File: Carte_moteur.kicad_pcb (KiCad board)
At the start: 2 copper layers, 111 parts, among them J101 Conn_01x02_Socket, J102 Conn_01x02, J103 Conn_01x02, J104 Conn_01x07, J105 Conn_01x02_Socket, J106 Conn_01x07, J201 Conn_01x05_Pin, J202 Conn_01x04_Pin, J301 Conn_01x05_Pin, J302 Conn_01x04_Pin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

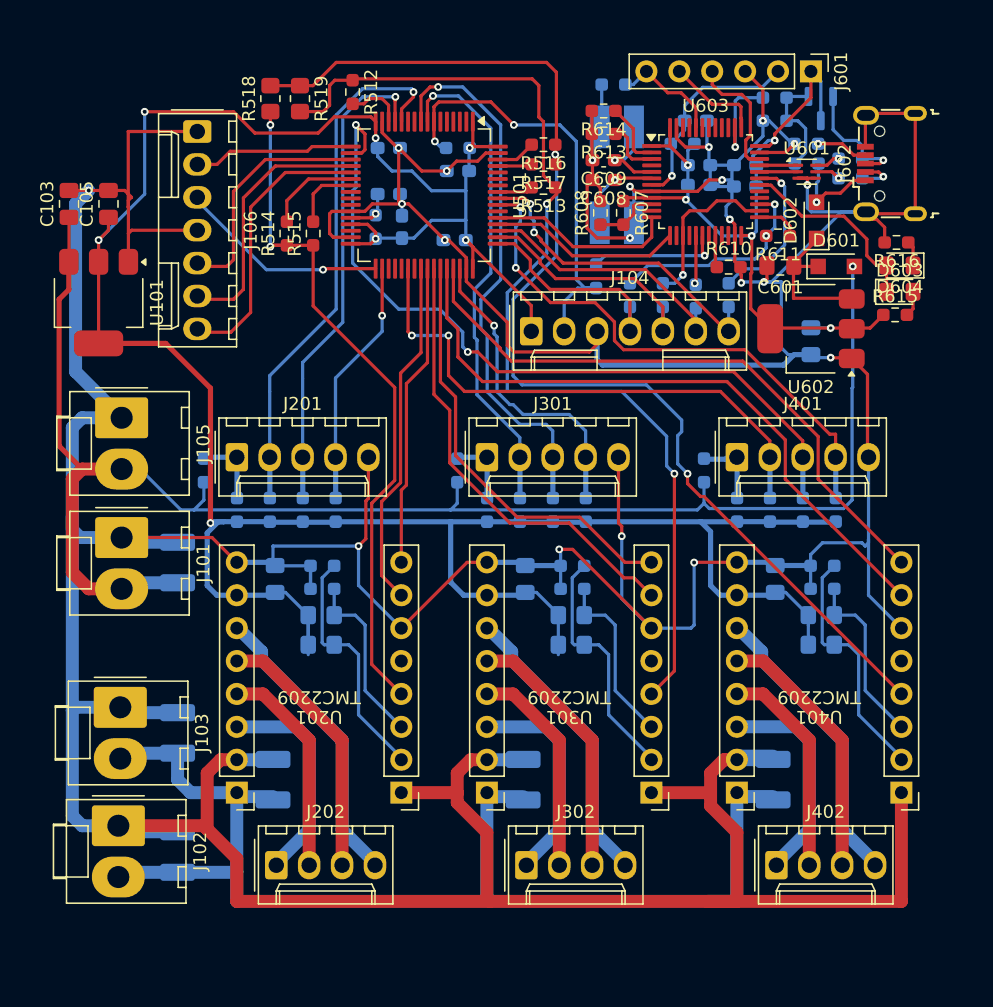
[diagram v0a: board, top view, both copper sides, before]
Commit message: silk and holes ok
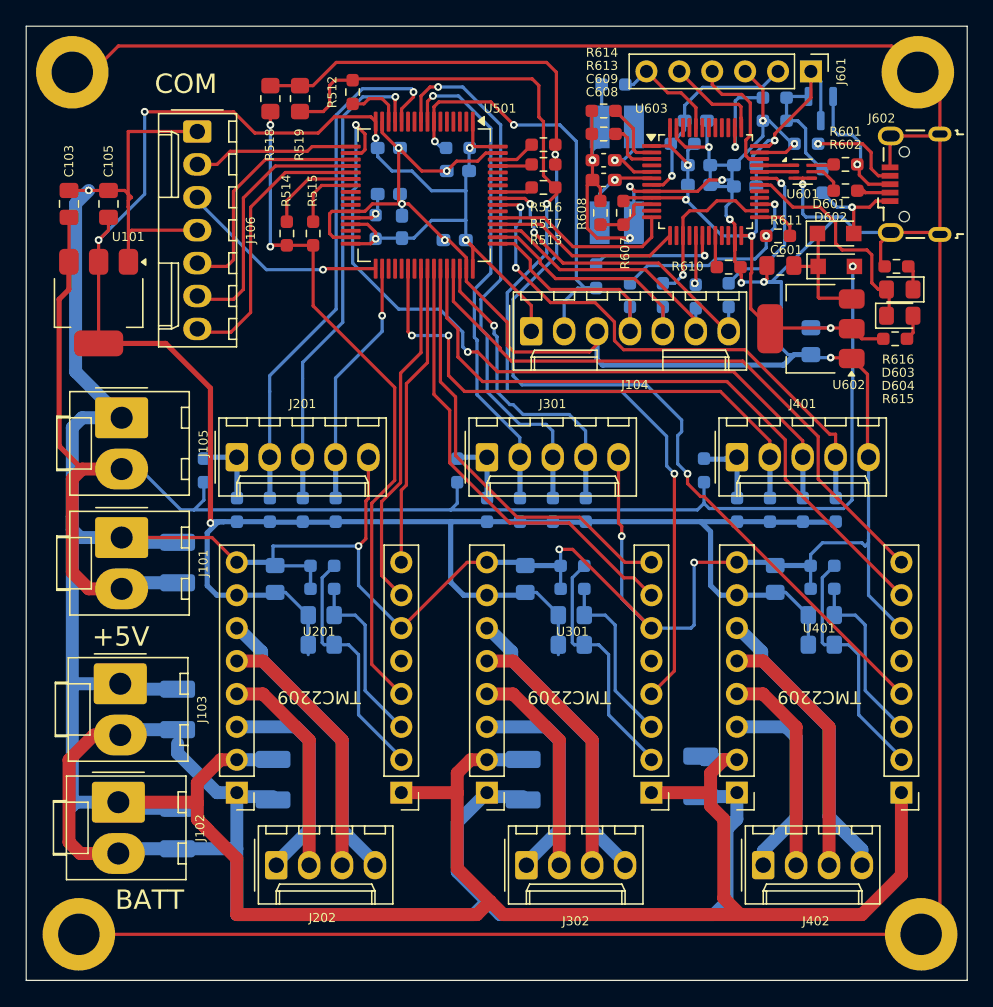
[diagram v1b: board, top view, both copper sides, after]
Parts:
- added H101: MountingHole_Pad, MountingHole:MountingHole_3.2mm_M3_DIN965_Pad, F.Cu at (79.5, 97.0)
- added H102: MountingHole_Pad, MountingHole:MountingHole_3.2mm_M3_DIN965_Pad, F.Cu at (144.8, 97.0)
- added H103: MountingHole_Pad, MountingHole:MountingHole_3.2mm_M3_DIN965_Pad, F.Cu at (80.0, 163.6)
- added H104: MountingHole_Pad, MountingHole:MountingHole_3.2mm_M3_DIN965_Pad, F.Cu at (145.0, 163.6)
- R601, R602: moved to F.Cu
- moved C401 5.59 mm to (128.0, 151.4)
- moved J602 2.48 mm to (144.5, 105.7)
- moved D603 1.85 mm to (143.4, 115.8)
- moved D604 1.85 mm to (143.4, 113.8)
- moved R615 1.85 mm to (143.0, 117.6)
- moved R616 1.85 mm to (143.1, 112.0)
- moved J103 1.82 mm to (83.2, 144.2)
- moved C102 1.82 mm to (87.6, 146.2)
- moved C104 1.82 mm to (87.6, 155.4)
- moved J102 1.82 mm to (83.1, 153.4)
- moved R604 1.81 mm to (137.4, 105.4), turned to 90 degrees
- moved D602 1.79 mm to (138.4, 109.5), turned to 0 degrees
- moved R602 1.03 mm to (139.2, 106.2)
- moved J402 1.02 mm to (132.8, 158.2)
- moved R601 0.59 mm to (139.2, 104.1)
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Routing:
- net GND: track 561.1 -> 743.8 mm
- net +BATT: track 91.1 -> 110.2 mm
- net Net-(J602-ID): track 4.01 -> 7.31 mm
- net Net-(D601-K): track 11.7 -> 8.97 mm
- net /stlink/LED: track 15.1 -> 17.1 mm
- net Net-(J602-D+): track 10.1 -> 10.8 mm
- net /tmc_motor2/A02: track 16.4 -> 15.7 mm
- net Net-(U601-D+_out): track 1.99 -> 1.33 mm, vias 1 -> 0
- net Net-(Q601-B): track 8.14 -> 8.74 mm
- net Net-(U601-D-_out): track 1.99 -> 2.39 mm, vias 1 -> 0
- net Net-(J602-D-): track 3.21 -> 2.95 mm, vias 1 -> 0
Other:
- board outline added: 72.6 x 73.7 mm
- board text added: "+5V"
- board text added: "BATT"
- board text added: "COM"

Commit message: ready for manufacturing
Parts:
- moved R518 1.65 mm to (94.8, 97.4)
- moved R519 1.65 mm to (97.1, 97.4)
- moved R512 0.51 mm to (101.1, 98.0)
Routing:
- net GND: track 743.8 -> 1265.2 mm, vias 21 -> 67
- net /micro/TMC1: track 53.9 -> 61.2 mm
- net /micro/TMC2: track 80.7 -> 78.3 mm
- net /micro/TMC3: track 91.8 -> 89.5 mm
- net /micro/TIM3_CH1: track 42.3 -> 44.5 mm
- net /micro/HRTIM_CHA1: track 35.3 -> 37.1 mm
- net /micro/TIM3_CH2: track 59.7 -> 61.3 mm
- net /micro/HRTIM_CHA2: track 33.4 -> 34.8 mm
- net /micro/T_SWDIO: track 17.5 -> 16.2 mm
- net /micro/TIM1_ETR: track 24.0 -> 22.8 mm
- net /micro/TIM5_CH1: track 41.3 -> 42.4 mm
- net /micro/T_SWCLK: track 19.7 -> 18.7 mm
- net /micro/SPI1_SCK: track 18.1 -> 19.0 mm
- net /micro/HRTIM_CHB1: track 50.8 -> 51.6 mm
- net /micro/TIM1_CH2: track 42.7 -> 42.1 mm
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- added copper zone on B.Cu, net GND
- added copper zone on F.Cu, net GND

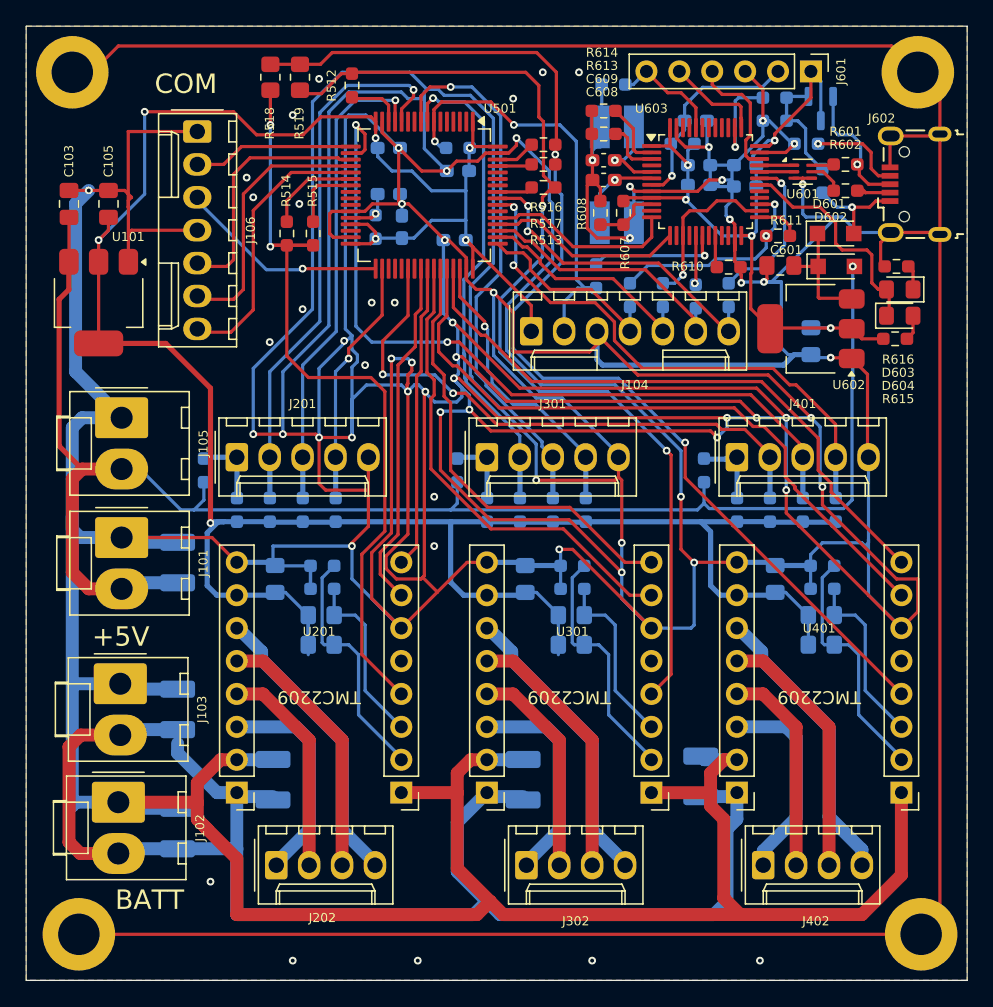
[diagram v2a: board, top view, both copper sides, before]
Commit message: remove wierd angles
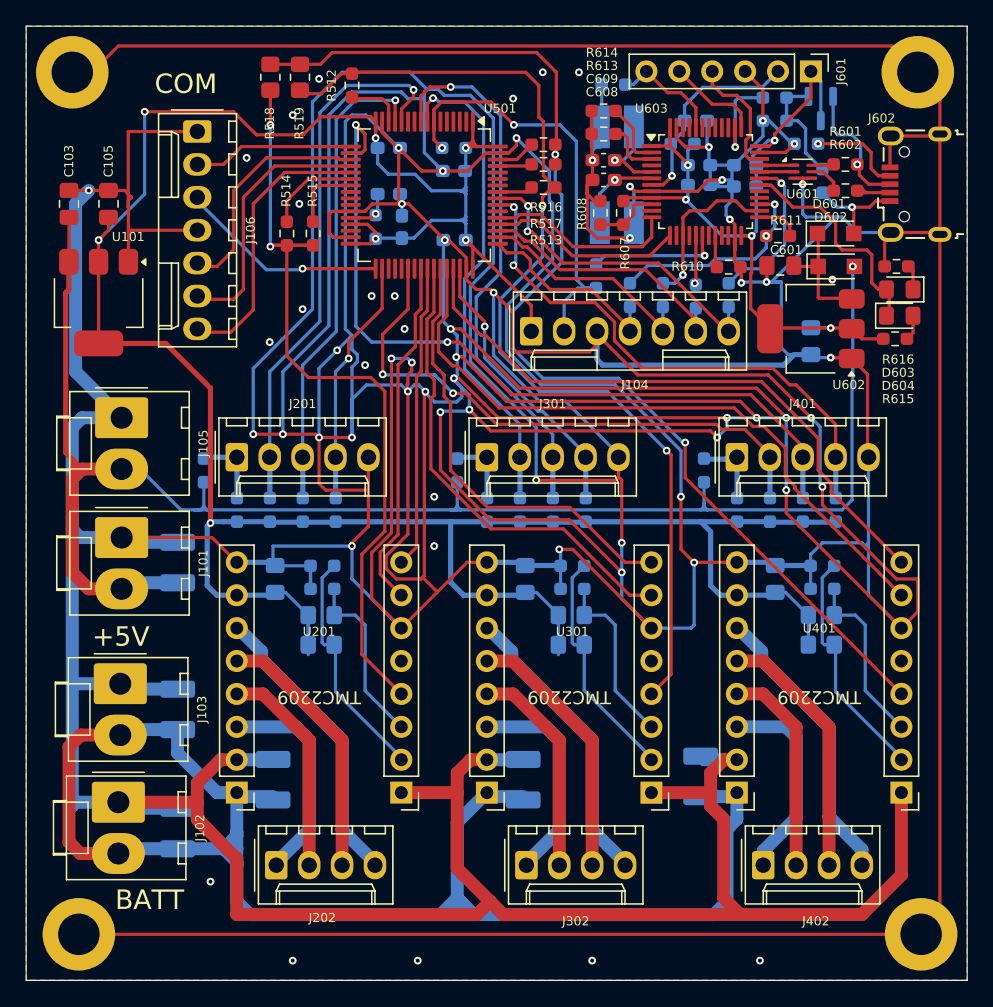
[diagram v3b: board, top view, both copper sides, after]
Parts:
- moved C503 0.31 mm to (109.0, 104.6)
- moved R510 0.31 mm to (109.0, 102.9)
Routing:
- net +BATT: track 110.8 -> 117.8 mm
- net +5V: track 121.4 -> 125.6 mm
- net +3V3: track 205.9 -> 209.4 mm
- net /micro/SPI1_SCK: track 19.0 -> 17.8 mm
- net /micro/TIM1_ETR: track 22.8 -> 21.9 mm
- net Net-(U301-MS1): track 19.1 -> 18.4 mm
- net Net-(U401-MS1): track 19.1 -> 18.5 mm
- net Net-(U201-MS1): track 19.1 -> 18.5 mm
- net GND: track 1265.2 -> 1264.8 mm, vias 67 -> 68
